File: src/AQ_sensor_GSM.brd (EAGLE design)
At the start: 47 x 64 mm, 52 parts, among them IC2 MCP73831/OT, J1 F-1X03-SIP-100-32, SW1 PCM12SMTR, U2 TEXAS_INSTRUMENTS_SN74HC125TE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, U3 TEXAS_INSTRUMENTS_LM1117IMP-3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, U4 ESP8266-12E/ESP-12E, U5 CH340G, X1 53048-08, X2 SIMLOCK-C707_10M006_512_2, X4 50 Ohms

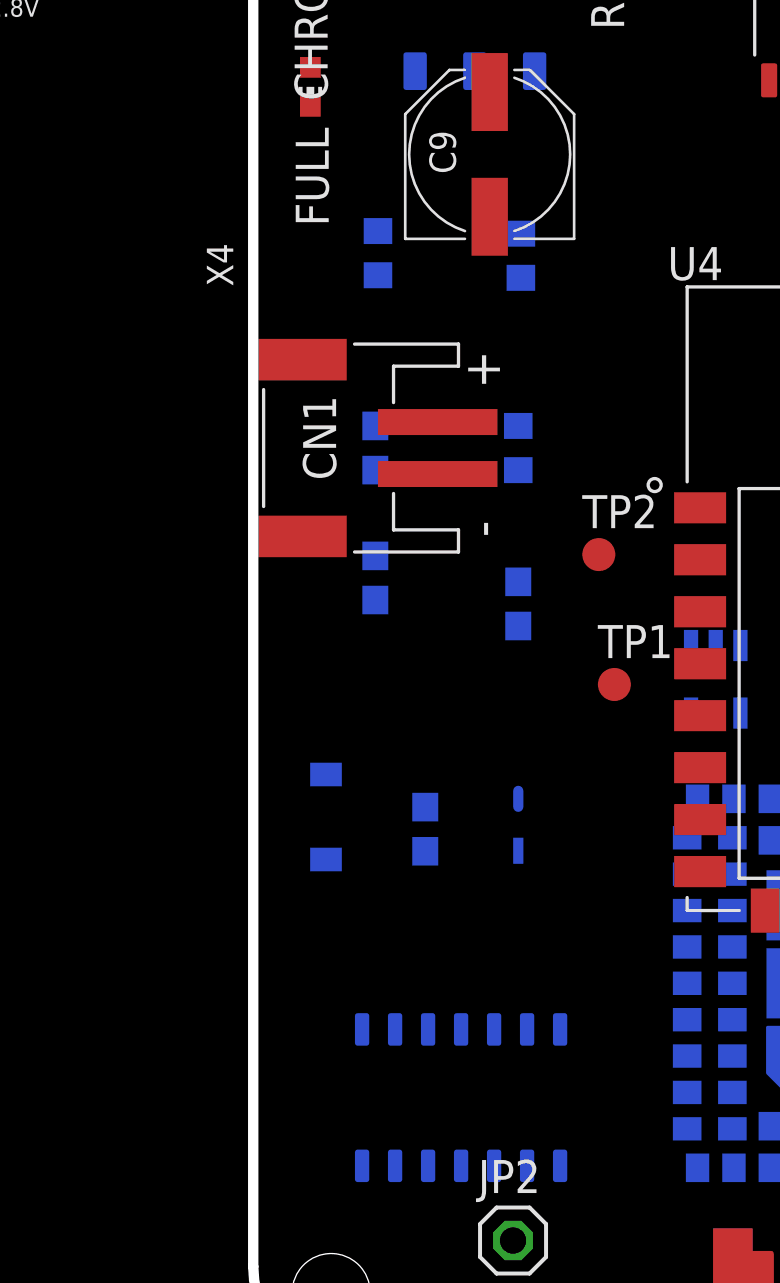
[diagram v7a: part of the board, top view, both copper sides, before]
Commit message: Routed Minus Rasnet
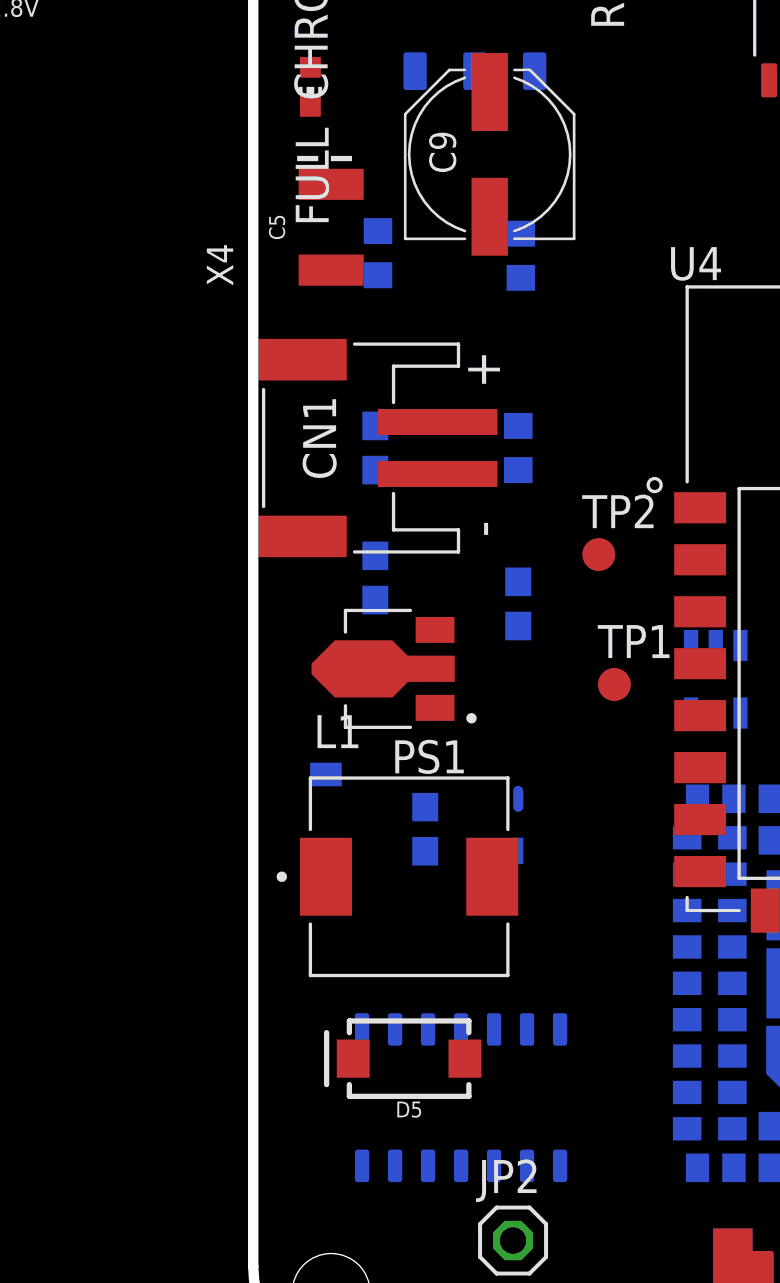
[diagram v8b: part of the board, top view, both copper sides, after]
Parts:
- added C5: 47uF, SparkFun-Capacitors:EIA3528
- added D5: 3A/40V/500mV, SparkFun-DiscreteSemi:SMA-DIODE
- added L1: B1047AS-470M=P3, B1047AS-470M_P3:IND_B1047AS-470M=P3
- added PS1: ME2108A33P, ME2108A33P:CONV_ME2108A33P
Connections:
- removed net VIN: MICRO_USB.1, SW1.2
- new net 5V_REG: C5.A, D5.C, PS1.2
- new net N$1: D5.A, L1.2, PS1.3
- net +5V: now also MICRO_USB.1; no longer SW1.1
- net GND: now also C5.C, PS1.1; no longer SW1.S1, SW1.S2, SW1.S3, SW1.S4
- net V_LIPO: now also L1.1
